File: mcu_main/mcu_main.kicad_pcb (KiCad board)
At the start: 2 copper layers, 108 x 61.7 mm, 48 parts, among them J1 Micro_SD_Card_Det_Hirose_DM3AT, J10 Conn_01x02_Pin, J2 Conn_01x10_Pin, J3 Conn_01x06_Pin, J4 4P4C_Shielded, J5 4P4C_Shielded, J6 Screw_Terminal_01x03_ebrake, J7 Screw_Terminal_01x03_throttle, J8 Screw_Terminal_01x06, J9 Conn_01x14_Socket, U1 ESP32-S3-WROOM-1, U2 USB_C_connector, U3 SGM2212-3.3, U4 VL53L1CXV0FY1, sw1 SW_Push_Dual, sw2 SW_Push_Dual

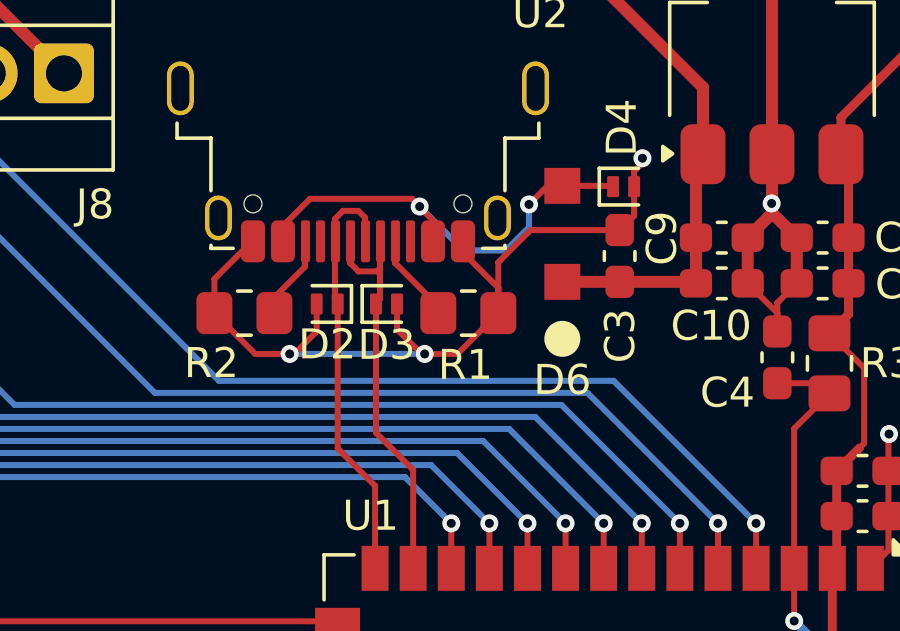
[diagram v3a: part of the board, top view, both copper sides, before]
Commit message: length matched usb data traces
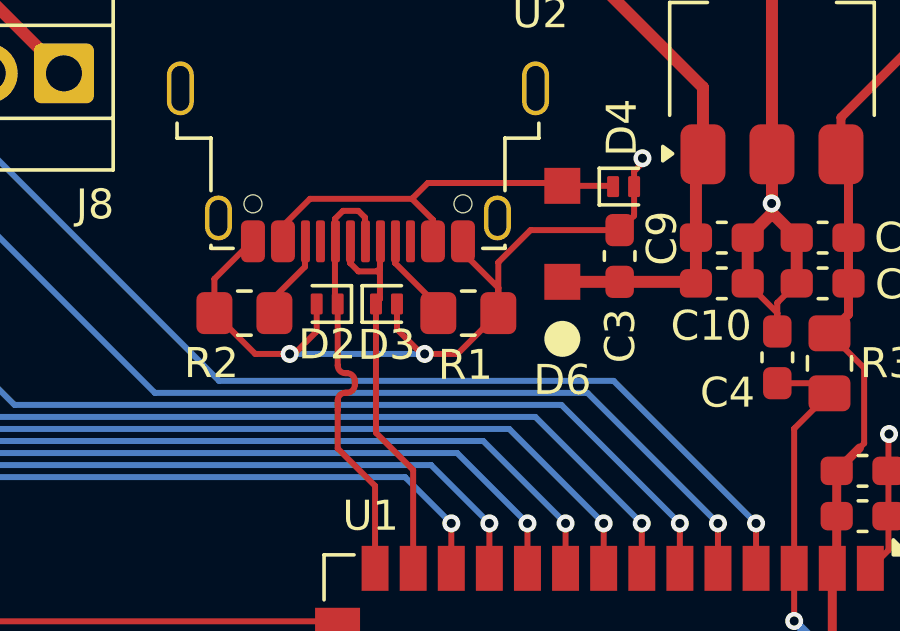
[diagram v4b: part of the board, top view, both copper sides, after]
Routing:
- net Net-(D6-A): track 15.3 -> 13.9 mm, vias 2 -> 0
- net /ESP USB section/D+: track 14.2 -> 14.8 mm
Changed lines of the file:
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@@
+	)
+	(segment
+		(start 177.763773 82.523033)
+		(end 177.67328 82.43254)
+		(width 0.2)
+		(layer "F.Cu")
+		(net 7)
+	)
+	(segment
+		(start 179.01 88.62)
+		(end 179.01 91.37)
+		(width 0.2)
+		(layer "F.Cu")
+		(net 7)
+	)
+	(segment
+		(start 178.67328 79.673546)
+		(end 178.67328 80.454317)
+		(width 0.2)
+		(layer "F.Cu")
+		(net 7)
+	)
+	(segment
+		(start 177.763773 85.775229)
+		(end 177.763773 85.905229)
+		(width 0.2)
+		(layer "F.Cu")
+		(net 7)
+	)
+	(segment
+		(start 177.67328 82.43254)
+		(end 177.67328 80.454317)
+		(width 0.2)
+		(layer "F.Cu")
+		(net 7)
+	)
+	(segment
+		(start 177.763773 85.905229)
+		(end 177.763773 86.08633)
+		(width 0.2)
+		(layer "F.Cu")
+		(net 7)
+	)
+	(segment
+		(start 178.453051 79.453317)
+		(end 178.67328 79.673546)
+		(width 0.2)
+		(layer "F.Cu")
+		(net 7)
+	)
+	(segment
+		(start 177.67328 80.454317)
+		(end 177.67328 79.720493)
+		(width 0.2)
+		(layer "F.Cu")
+		(net 7)
+	)
+	(segment
+		(start 178.073773 85.515229)
+		(end 178.023773 85.515229)
+		(width 0.2)
+		(layer "F.Cu")
+		(net 7)
+	)
+	(segment
+		(start 177.763773 86.08633)
+		(end 177.763773 87.373773)
+		(width 0.2)
+		(layer "F.Cu")
+		(net 7)
 	)
 	(segment
@@
 	)
 	(segment
-		(start 177.763773 82.523033)
-		(end 177.67328 82.43254)
-		(width 0.2)
-		(layer "F.Cu")
-		(net 7)
-	)
-	(segment
-		(start 179.01 88.62)
-		(end 179.01 91.37)
-		(width 0.2)
-		(layer "F.Cu")
-		(net 7)
-	)
-	(segment
-		(start 178.67328 79.673546)
-		(end 178.67328 80.454317)
-		(width 0.2)
-		(layer "F.Cu")
-		(net 7)
-	)
-	(segment
-		(start 177.67328 82.43254)
-		(end 177.67328 80.454317)
-		(width 0.2)
-		(layer "F.Cu")
-		(net 7)
-	)
-	(segment
-		(start 178.453051 79.453317)
-		(end 178.67328 79.673546)
-		(width 0.2)
-		(layer "F.Cu")
-		(net 7)
-	)
-	(segment
-		(start 177.67328 80.454317)
-		(end 177.67328 79.720493)
-		(width 0.2)
-		(layer "F.Cu")
-		(net 7)
-	)
-	(segment
-		(start 177.763773 82.557357)
-		(end 177.763773 87.373773)
-		(width 0.2)
-		(layer "F.Cu")
-		(net 7)
-	)
-	(segment
 		(start 177.940456 79.453317)
 		(end 178.453051 79.453317)
@@
 	)
 	(segment
+		(start 177.763773 82.557357)
+		(end 177.763773 84.605229)
+		(width 0.2)
+		(layer "F.Cu")
+		(net 7)
+	)
+	(segment
+		(start 178.023773 84.865229)
+		(end 178.073773 84.865229)
+		(width 0.2)
+		(layer "F.Cu")
+		(net 7)
+	)
+	(segment
 		(start 177.67328 79.720493)
 		(end 177.940456 79.453317)
@@
 	)
 	(segment
+		(start 178.333773 85.125229)
+		(end 178.333773 85.255229)
+		(width 0.2)
+		(layer "F.Cu")
+		(net 7)
+	)
+	(arc
+		(start 178.023773 85.515229)
+		(mid 177.839925 85.591381)
+		(end 177.763773 85.775229)
+		(width 0.2)
+		(layer "F.Cu")
+		(net 7)
+	)
+	(arc
+		(start 177.763773 84.605229)
+		(mid 177.839925 84.789077)
+		(end 178.023773 84.865229)
+		(width 0.2)
+		(layer "F.Cu")
+		(net 7)
+	)
+	(arc
+		(start 178.333773 85.255229)
+		(mid 178.257621 85.439077)
+		(end 178.073773 85.515229)
+		(width 0.2)
+		(layer "F.Cu")
+		(net 7)
+	)
+	(arc
+		(start 178.073773 84.865229)
+		(mid 178.257621 84.941381)
+		(end 178.333773 85.125229)
+		(width 0.2)
+		(layer "F.Cu")
+		(net 7)
+	)
+	(segment
 		(start 179.17328 81.37)
 		(end 179.17328 82.390297)
@@
 	)
 	(segment
-		(start 180.92328 79.754317)
-		(end 180.92328 80.454317)
-		(width 0.2)
-		(layer "F.Cu")
-		(net 9)
-	)
-	(segment
-		(start 184.76 78.62)
-		(end 184.140311 79.239689)
-		(width 0.2)
-		(layer "F.Cu")
-		(net 9)
-	)
-	(segment
 		(start 176.841456 79.052317)
 		(end 175.92328 79.970493)
@@
 	)
 	(segment
-		(start 180.497442 79.30962)
+		(start 180.767386 78.52507)
 		(end 180.240139 79.052317)
 		(width 0.2)
@@
 	)
 	(segment
-		(start 180.497442 79.328479)
-		(end 180.92328 79.754317)
+		(start 185.156864 78.52507)
+		(end 180.767386 78.52507)
 		(width 0.2)
 		(layer "F.Cu")
@@
 	)
 	(segment
+		(start 180.94 79.752178)
+		(end 180.240139 79.052317)
+		(width 0.2)
+		(layer "F.Cu")
+		(net 9)
+	)
+	(segment
 		(start 185.251794 78.62)
-		(end 184.76 78.62)
+		(end 185.156864 78.52507)
 		(width 0.2)
 		(layer "F.Cu")
@@
 	)
 	(segment
-		(start 180.497442 79.30962)
-		(end 180.497442 79.328479)
+		(start 180.94 80.47)
+		(end 180.94 79.752178)
 		(width 0.2)
 		(layer "F.Cu")
@@
 		(width 0.2)
 		(layer "F.Cu")
-		(net 9)
-	)
-	(via
-		(at 184.140311 79.239689)
-		(size 0.6)
-		(drill 0.3)
-		(layers "F.Cu" "B.Cu")
-		(net 9)
-	)
-	(via
-		(at 180.497442 79.30962)
-		(size 0.6)
-		(drill 0.3)
-		(layers "F.Cu" "B.Cu")
-		(net 9)
-	)
-	(segment
-		(start 184.140311 79.239689)
-		(end 184.140311 80.001763)
-		(width 0.2)
-		(layer "B.Cu")
-		(net 9)
-	)
-	(segment
-		(start 184.140311 80.001763)
-		(end 183.369041 80.773033)
-		(width 0.2)
-		(layer "B.Cu")
-		(net 9)
-	)
-	(segment
-		(start 183.369041 80.773033)
-		(end 181.960855 80.773033)
-		(width 0.2)
-		(layer "B.Cu")
-		(net 9)
-	)
-	(segment
-		(start 181.960855 80.773033)
-		(end 180.497442 79.30962)
-		(width 0.2)
-		(layer "B.Cu")
 		(net 9)
 	)
@@
 		)
 	)
+	(generated
+		(type tuning_pattern)
+		(name "Tuning Pattern")
+		(layer "F.Cu")
+		(base_line
+			(pts
+				(xy 177.763773 84.605229) (xy 177.763773 86.08633)
+			)
+		)
+		(corner_radius_percent 80)
+		(end
+			(xy 177.763773 86.08633)
+		)
+		(initial_side "left")
+		(last_diff_pair_gap 0.18)
+		(last_netname "/ESP USB section/D+")
+		(last_status "tuned")
+		(last_track_width 0.2)
+		(last_tuning "10.0224 mm (tuned)")
+		(max_amplitude 0.57)
+		(min_amplitude 0.2)
+		(min_spacing 0.65)
+		(origin
+			(xy 177.763773 84.605229)
+		)
+		(override_custom_rules no)
+		(rounded yes)
+		(single_sided no)
+		(target_length 1000000)
+		(target_length_max 1000000)
+		(target_length_min 0)
+		(target_skew 0)
+		(target_skew_max 0.1)
+		(target_skew_min -0.1)
+		(tuning_mode "single")
+		(members "066541a9-0f39-403d-a60a-e0cfa59650a6" "1633e46e-521b-4a1b-b7b7-6dcb25b3424f"
+			"34849b8f-1204-4f0a-8472-50b94d7b00b4" "469a8342-faad-4f0d-8f6b-ab4a2509cc70"
+			"708bde3f-7ff2-41ab-bb8e-fad83b93da93" "8ed08741-399e-4f29-b9af-b39cf303c07b"
+			"bd12bd3d-4ec9-4921-b238-0de4f7d0d664" "daf4f081-9f9c-4018-a78a-b23a5488d30d"
+			"f535e0f8-762a-45bb-9e01-ea0f0af422b1"
+		)
+	)
